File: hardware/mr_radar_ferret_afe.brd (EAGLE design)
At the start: 26 x 46 mm, 34 parts, among them U16 AD7276, U18 REF2930, U5 MAX9812, U6 MAX9812, U9 MAX7410

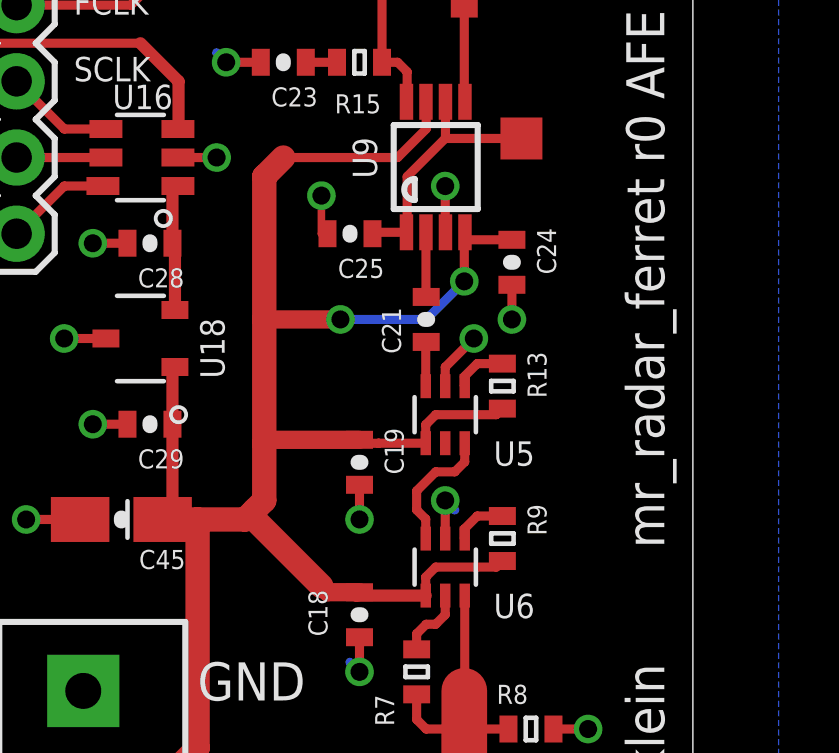
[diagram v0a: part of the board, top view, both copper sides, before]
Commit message: currently tested ferret r0, fixing a few bugs for the next revision, board layout of ferret now incomplete. isolation is much better than in platypus, but it is still a problem
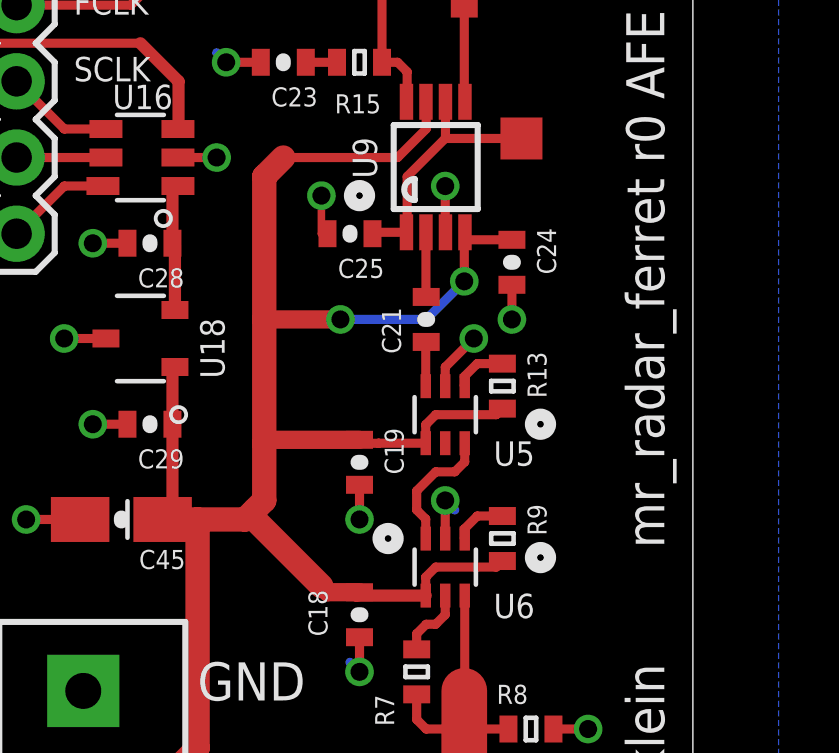
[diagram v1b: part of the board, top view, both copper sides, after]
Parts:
- C23: value 2nH -> 22pF
- R16: value JMP -> DNP
- R6, R8: value 100 -> DNP
- R7: value 2k -> DNP
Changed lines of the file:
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@@
 <layer number="33" name="tFinish" color="6" fill="3" visible="no" active="yes"/>
 <layer number="34" name="bFinish" color="6" fill="6" visible="no" active="yes"/>
-<layer number="35" name="tGlue" color="7" fill="4" visible="no" active="yes"/>
+<layer number="35" name="tGlue" color="7" fill="4" visible="yes" active="yes"/>
 <layer number="36" name="bGlue" color="7" fill="5" visible="no" active="yes"/>
 <layer number="37" name="tTest" color="7" fill="1" visible="no" active="yes"/>
@@
 <wire x1="66.04" y1="15.24" x2="66.04" y2="61.2775" width="0.0254" layer="20"/>
 <wire x1="66.04" y1="61.2775" x2="40.005" y2="61.2775" width="0.0254" layer="20"/>
+<circle x="54.9275" y="43.18" radius="0.3175" width="0.4064" layer="121"/>
+<circle x="55.88" y="31.75" radius="0.3175" width="0.4064" layer="121"/>
+<circle x="60.96" y="31.115" radius="0.3175" width="0.4064" layer="121"/>
+<circle x="60.96" y="35.56" radius="0.3175" width="0.4064" layer="121"/>
 </plain>
 <attributes>
@@
 </element>
 <element name="J$3" library="SparkFun-Connectors" package="SMA-EDGE" value="SMA_EDGE" x="60.96" y="59.055" rot="R180"/>
-<element name="R6" library="pel_dipol_comp" package="0603-RES" value="100" x="60.6425" y="21.59"/>
+<element name="R6" library="pel_dipol_comp" package="0603-RES" value="DNP" x="60.6425" y="21.59"/>
 <element name="C10" library="pel_dipol_comp" package="3216/A" value="10uF" x="58.42" y="22.86" smashed="yes" rot="R90">
 <attribute name="NAME" x="57.0865" y="22.9489" size="0.635" layer="25" font="vector" ratio="16" rot="R90"/>
@@
 </element>
 <element name="R14" library="pel_dipol_comp" package="0603-RES" value="JMP" x="58.42" y="50.165" rot="R270"/>
-<element name="C23" library="pel_dipol_comp" package="0603-CAP" value="2nH" x="52.3875" y="47.625" rot="R180"/>
+<element name="C23" library="pel_dipol_comp" package="0603-CAP" value="22pF" x="52.3875" y="47.625" rot="R180"/>
 <element name="R15" library="pel_dipol_comp" package="0603-RES" value="JMP" x="54.9275" y="47.625" smashed="yes">
 <attribute name="NAME" x="54.102" y="45.9232" size="0.635" layer="25" font="vector" ratio="16"/>
 <attribute name="VALUE" x="53.7845" y="46.3296" size="0.635" layer="27" font="vector" ratio="16"/>
 </element>
-<element name="R16" library="pel_dipol_comp" package="0603-RES" value="JMP" x="54.9275" y="50.165" smashed="yes" rot="R180">
+<element name="R16" library="pel_dipol_comp" package="0603-RES" value="DNP" x="54.9275" y="50.165" smashed="yes" rot="R180">
 <attribute name="NAME" x="53.5305" y="50.5968" size="0.635" layer="25" font="vector" ratio="16" rot="R180"/>
 <attribute name="VALUE" x="56.0705" y="51.4604" size="0.635" layer="27" font="vector" ratio="16" rot="R180"/>
 </element>
 <element name="C24" library="pel_dipol_comp" package="0603-CAP" value="100nF" x="60.0075" y="40.9575" rot="R270"/>
-<element name="R7" library="pel_dipol_comp" package="0603-RES" value="2k" x="56.8325" y="27.305" smashed="yes" rot="R270">
+<element name="R7" library="pel_dipol_comp" package="0603-RES" value="DNP" x="56.8325" y="27.305" smashed="yes" rot="R270">
 <attribute name="NAME" x="55.4482" y="26.543" size="0.635" layer="25" font="vector" ratio="16" rot="R270"/>
 <attribute name="VALUE" x="55.5371" y="28.448" size="0.635" layer="27" font="vector" ratio="16" rot="R270"/>
@@
 </element>
 <element name="J$6" library="SparkFun-Connectors" package="SMA-EDGE" value="SMA_EDGE" x="60.96" y="17.4625" rot="R180"/>
-<element name="R8" library="pel_dipol_comp" package="0603-RES" value="100" x="60.6425" y="25.4"/>
+<element name="R8" library="pel_dipol_comp" package="0603-RES" value="DNP" x="60.6425" y="25.4"/>
 <element name="JP4" library="SparkFun-Connectors" package="SCREWTERMINAL-3.5MM-3" value="" x="45.72" y="26.67" smashed="yes" rot="R270">
 <attribute name="VALUE" x="46.99" y="27.94" size="0.4064" layer="27" rot="R270"/>
@@
 </signal>
 </signals>
-<errors>
-</errors>
 </board>
 </drawing>
